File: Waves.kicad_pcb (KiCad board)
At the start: 2 copper layers, 49.8 x 106.5 mm, 154 parts, among them J1 AudioJack2_SwitchT, J10 AudioJack2_SwitchT, J11 Conn_01x04_Male, J12 Conn_01x04_Male, J13 AudioJack2_SwitchT, J14 AudioJack2_SwitchT, J15 Conn_02x05_Odd_Even, J2 AudioJack2_SwitchT, J3 AudioJack2_SwitchT, J4 AudioJack2_SwitchT, J5 AudioJack2_SwitchT, J6 AudioJack2_SwitchT, J7 AudioJack2_SwitchT, J8 AudioJack2_SwitchT, J9 AudioJack2_SwitchT, Q1 BC847, Q2 BC847, Q3 BC847, Q4 BC847, Q5 BC847, Q6 BC847, SW1 SW_Push, SW2 Rotary_Encoder_Switch, SW3 SW_Push_LED, SW4 SW_Push_LED, SW5 SW_Push_LED, SW6 SW_Push_LED, U1 STM32G431, U2 AT25xxx, U3 IPS240x240, U4 PCM5100, U5 TL072, U6 LM1117-3.3, U7 LM1117-3.3, U8 MCP6004, U9 MCP6004, Y1 8MHz

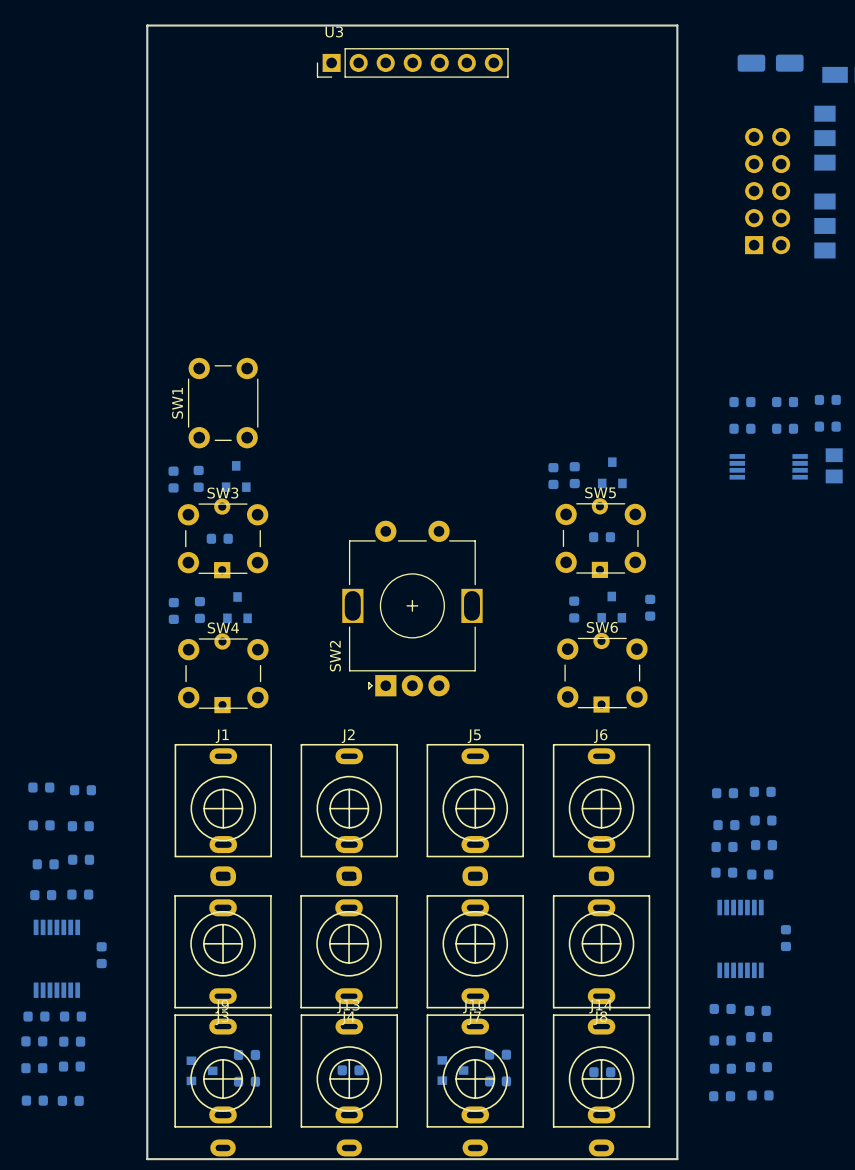
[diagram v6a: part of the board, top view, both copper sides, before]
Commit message: Placed ADC input stages.
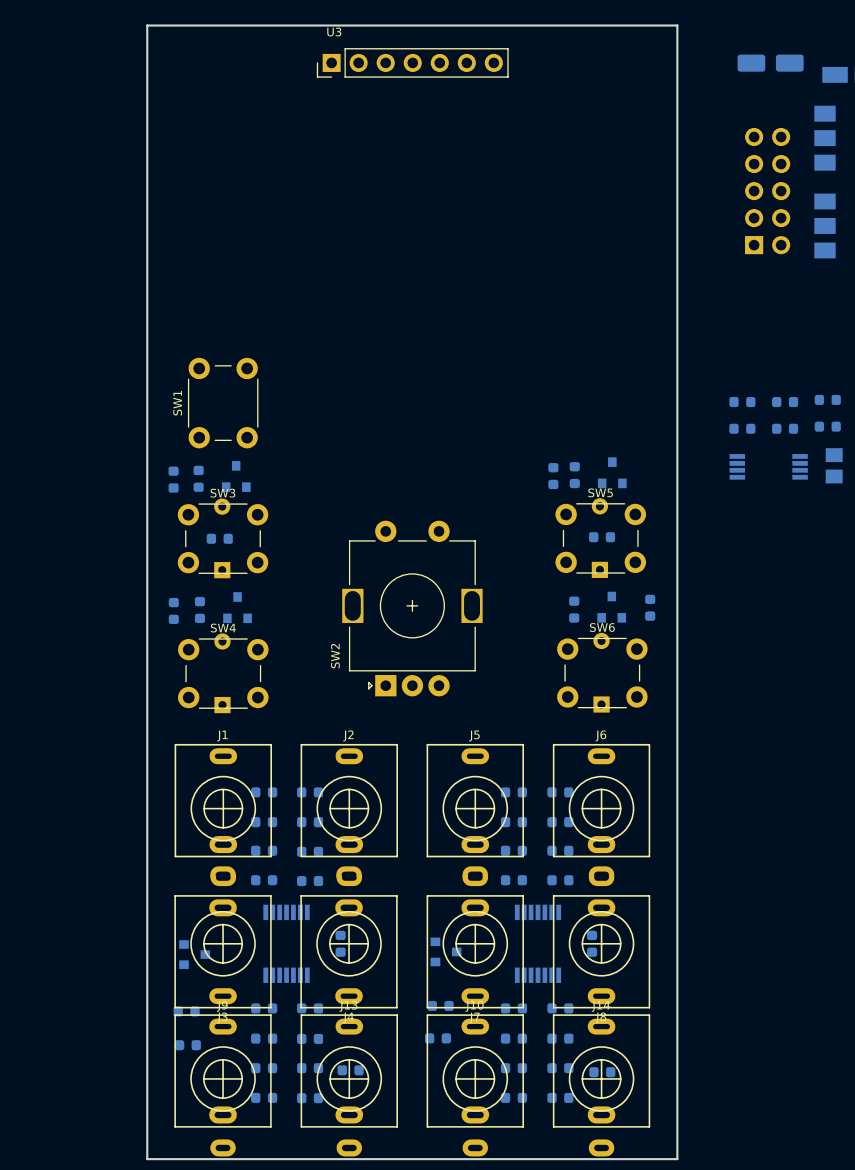
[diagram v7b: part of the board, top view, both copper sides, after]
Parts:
- moved R34 22.5 mm to (117.3, 149.1)
- moved C43 22.5 mm to (120.1, 134.6)
- moved R33 22.4 mm to (117.3, 146.3)
- moved C46 22.4 mm to (117.3, 143.6)
- moved R37 22.3 mm to (117.3, 140.7)
- moved R32 21.6 mm to (117.3, 128.7)
- moved U8 21.6 mm to (115.1, 134.6)
- moved C47 21.6 mm to (113.0, 143.5)
- moved R35 21.6 mm to (113.0, 146.3)
- moved R29 21.5 mm to (117.3, 123.2)
- moved R36 21.5 mm to (113.0, 149.1)
- moved C45 21.5 mm to (117.3, 126.0)
- moved R38 21.4 mm to (113.0, 140.7)
- moved R30 21.3 mm to (117.3, 120.4)
- moved R28 20.9 mm to (113.0, 120.4)
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
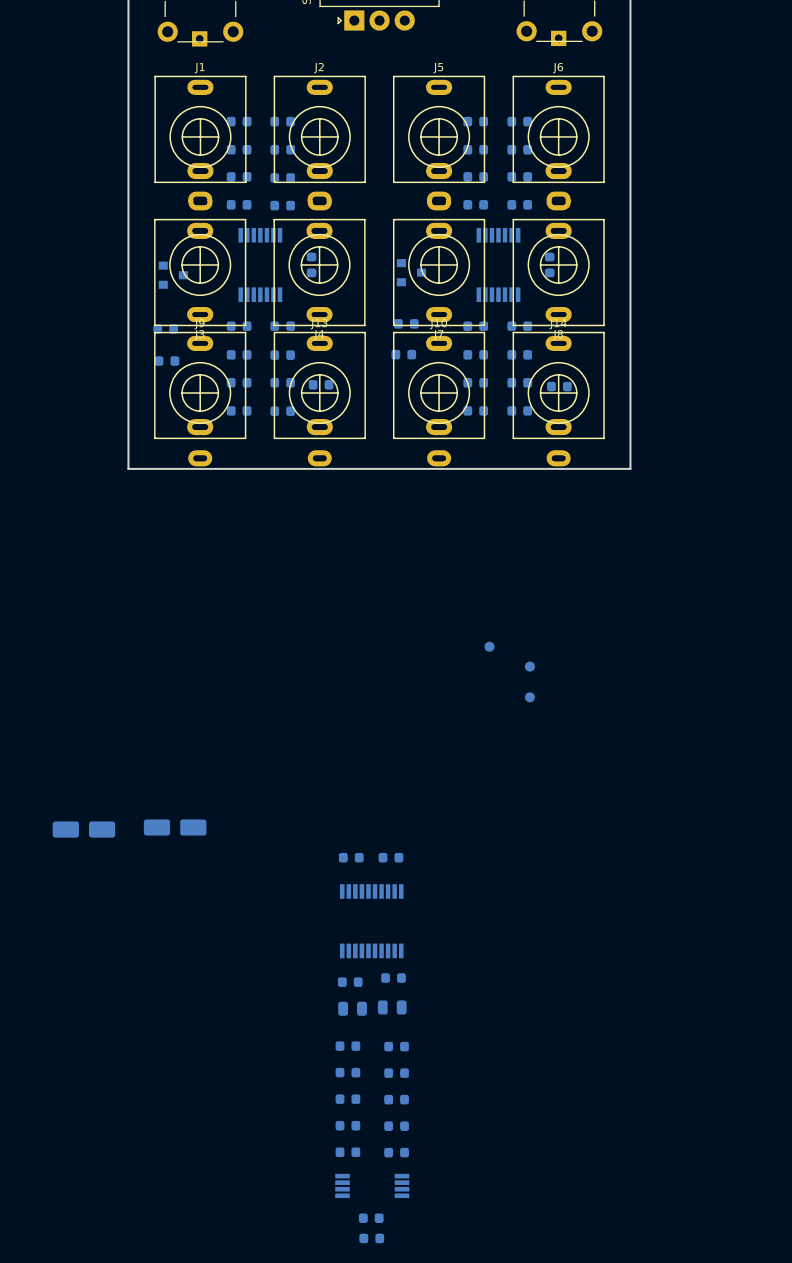
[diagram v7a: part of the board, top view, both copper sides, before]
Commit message: Placed DAC and output stage.
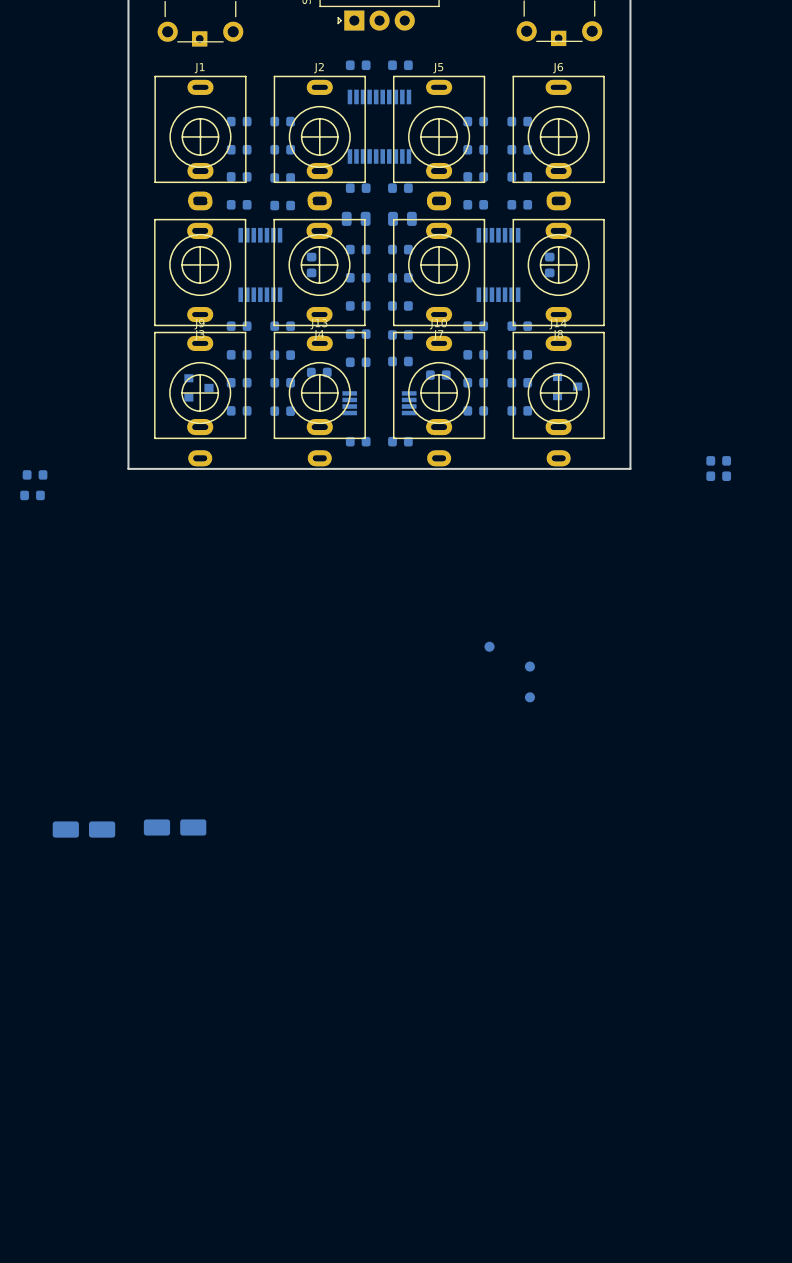
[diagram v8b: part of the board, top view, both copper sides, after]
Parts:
- moved C27 79.1 mm to (129.0, 152.1)
- moved R15 79.1 mm to (129.0, 133.1)
- moved R10 79.0 mm to (124.8, 133.1)
- moved C30 78.9 mm to (129.0, 135.9)
- moved C25 78.9 mm to (124.8, 135.9)
- moved U4 78.8 mm to (126.9, 120.9)
- moved C19 78.8 mm to (124.8, 127.0)
- moved R13 78.7 mm to (129.0, 138.7)
- moved R12 78.7 mm to (124.8, 138.7)
- moved C24 78.6 mm to (129.0, 114.8)
- moved C18 78.6 mm to (124.8, 114.8)
- moved C29 78.5 mm to (124.8, 141.5)
- moved C26 78.5 mm to (129.0, 141.6)
- moved R11 78.5 mm to (129.0, 144.2)
- moved R14 78.4 mm to (124.8, 144.3)
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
